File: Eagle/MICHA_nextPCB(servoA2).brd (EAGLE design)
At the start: 110.5 x 83.1 mm, 57 parts, among them IC1 LM4041A12LP, K1 PIN20X2, T1 BSS84, U1 ARDUINO_MKR_ZERO, U2 MIKROE_CLICK, X1 SS-7188S-A-NF_V2, X2 SS-7188S-A-NF_V2, X3 SS-7188S-A-NF_V2, X4 SS-7188S-A-NF_V2, X5 SS-7188S-A-NF_V2, X6 SS-7188S-A-NF_V2, X7 BUCHANAN_4_3.5MM

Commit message: Update for next PCB version
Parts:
- removed TVS3: 5Vdc/12pF, EMCComponents (rev19b):WE-TVS_SOT23-3L
- removed Z3, Z4: 3,3V, Zener_SMA:ZENER_SMA
- added O1: HMHA281R2, HMHA281R2:HMHA281R2
- added R18: 390, resistor:R1206
- added R19: 2k, resistor:R1206
- R1, R2: value 180 -> 100
- R12, R8, R9: device rcl:R1210 -> rcl:R1206
- R6: value 15-1/4W -> 680
- R7: value 15-1/4W -> 1k
- moved R7 54.8 mm to (49.5, 4.76), turned to 0 degrees
- moved R6 39.2 mm to (61.9, -0.95), turned to 180 degrees
- moved R8 11.1 mm to (106.4, -2.70), turned to 0 degrees
- moved Z1 5.29 mm to (99.1, -2.70)
- moved Z2 4.71 mm to (91.1, -2.70)
- moved R9 3.88 mm to (85.4, -0.95), turned to 90 degrees
- moved C6 3.70 mm to (78.7, 0.32)
- moved TBD2 3.70 mm to (78.7, 13.7)
- moved LS1 3.27 mm to (79.4, 35.9)
- moved C3 2.56 mm to (79.1, 46.5)
- moved C4 2.56 mm to (79.1, 50.0)
- moved R3 2.56 mm to (85.4, 46.5)
- moved R4 2.56 mm to (85.4, 50.0)
- moved C5 2.56 mm to (79.1, 53.3)
- moved R5 2.56 mm to (85.4, 53.3)
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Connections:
- removed net N$1: R17.2, T1.2, U1.J5_12
- removed net N$14: C13.1, R6.2, TVS3.2, U1.J4_4, Z3.C
- removed net PUMP_SERVO: R6.1, X4.6
- new net N$7: O1.P$1, R18.2
- new net N$9: C13.1, O1.P$4, R6.1, U1.J4_4
- new net PUMP_SERVO_A+: R18.1, X4.6
- new net PUMP_SERVO_A-: O1.P$2, X4.3
- new net VDD: R17.2, R6.2, T1.2, U1.J5_12
- net D19: now also R19.2; no longer TVS3.1, Z4.C
- net GND: now also O1.P$3, R19.1; no longer TVS3.3, X4.3, Z3.A, Z4.A
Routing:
- net N$14: track 87.9 -> 0.00 mm
- net D19: track 88.9 -> 17.2 mm
- net N$9: track 0.00 -> 67.4 mm, vias 0 -> 2
- net PUMP_ERR: track 2.23 -> 64.7 mm, vias 0 -> 1
- net VDD: track 0.00 -> 55.7 mm, vias 0 -> 1
- net TANK2_RELAY: track 4.79 -> 43.0 mm
- net N$1: track 29.2 -> 0.00 mm
- net N$4: track 18.7 -> 33.7 mm
- net PUMP_SERVO_A-: track 0.00 -> 13.9 mm
- net TX_PI: track 102.5 -> 91.3 mm, vias 1 -> 3
- net PUMP_SERVO_A+: track 0.00 -> 10.8 mm
- net PUMP_DIR: track 3.87 -> 11.3 mm
- net SOL_COLD: track 32.7 -> 39.4 mm
- net D2: track 29.1 -> 24.2 mm
- net PI_STATE_LED: track 38.5 -> 42.7 mm
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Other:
- board text added: "MICHA V1.1"
- board text removed: "MICHA V1.0"

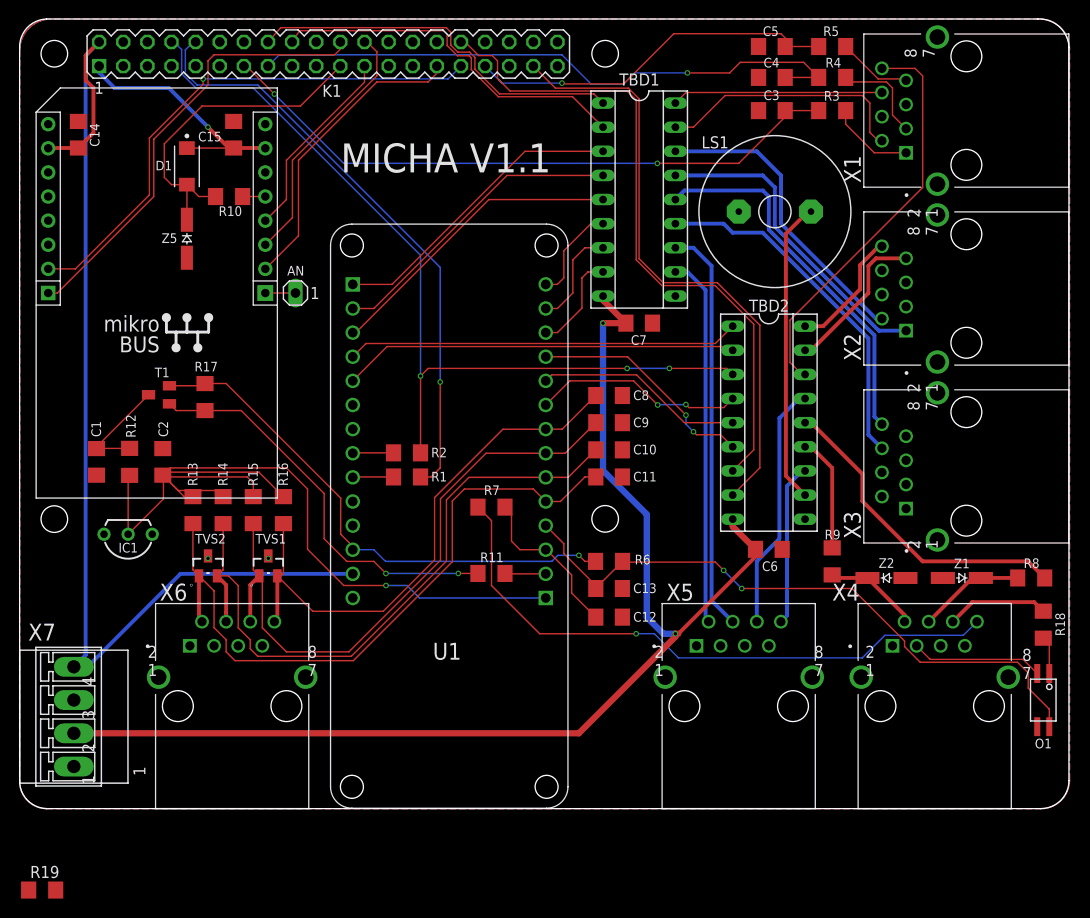
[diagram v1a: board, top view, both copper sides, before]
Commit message: MICHA_nextPCB updated
- analog switch added
- zener and tvs for protection added
- schottky diode deleted
- error signal go through a bridge divider instead of a zener
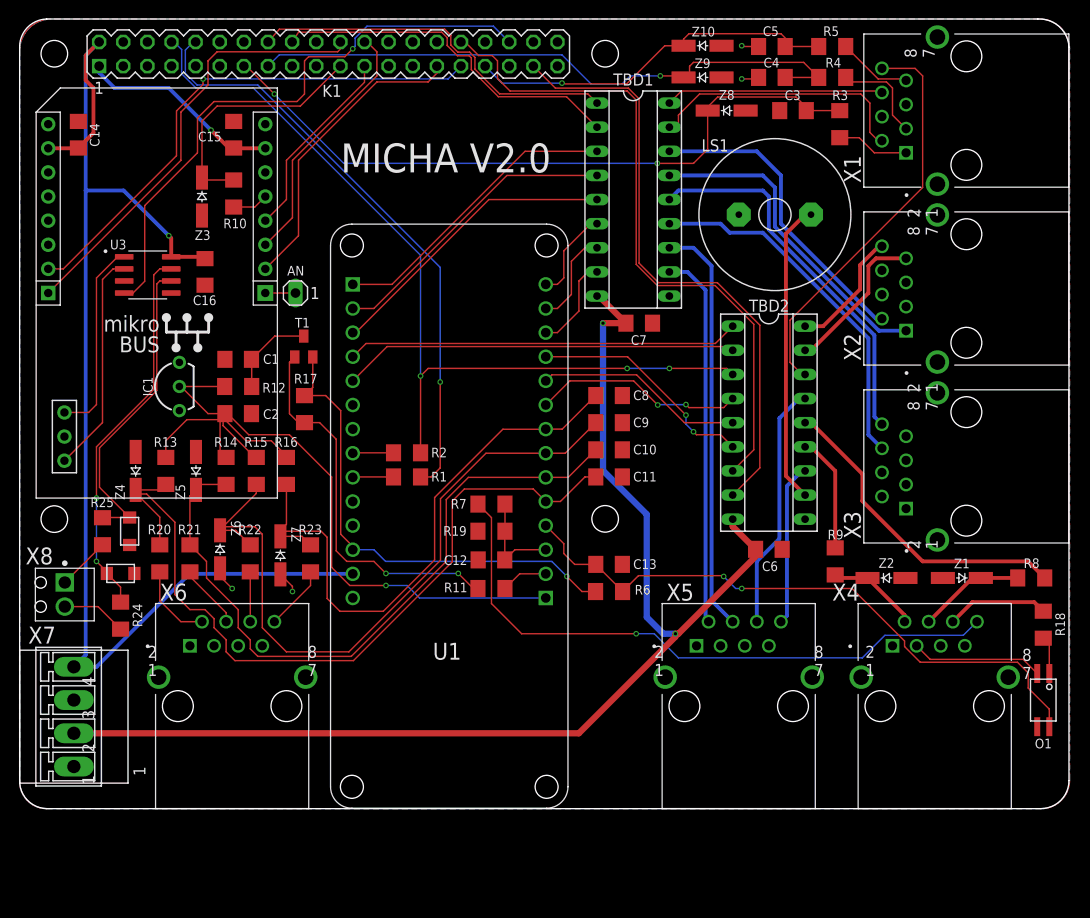
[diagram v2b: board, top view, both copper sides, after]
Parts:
- removed D1: STMICROELECTRONICS_STPS1L30ASTMICROELECTRONICS_STPS1L30A_0_0, Diode_STPS1L30A:STMICROELECTRONICS_STPS1L30A_0
- added C16: 100nF, rcl:C1206
- added R20, R21, R22, R23, R24, R25: 33, resistor:R1206
- added U3: MAX4528CSA, MAX4528CSA:SOIC127P600X175-8N
- added X8: MPT_0,5/_2-2,54_1725656_2, MPT_0_5__2-2_54_1725656:PH_MPT_0,5/_2-2,54_1725656
- added Z10, Z3, Z4, Z6, Z7, Z8, Z9: 3,3V, Zener_SMA:ZENER_SMA
- TVS1, TVS2: value 5Vdc/12pF -> TVS_SOD123; device EMCComponents (rev19b):WE-TVS_SOT23-3L -> TV02W6V0B-G_SOD123:TVS_SOD123
- U2: value MIKROE_CLICK -> MIKROE_CLICK_UPGRADE; device mikrobus_lib:MIKROE_BUS_MIDI_NOLABEL -> mikrobus_lib:MIKROE_BUS_MIDI_UPGRADE
- moved R19 60.5 mm to (49.5, 2.22)
- moved Z5 24.5 mm to (18.4, 8.57), turned to 90 degrees
- moved C1 18.4 mm to (22.9, 20.3), turned to 180 degrees
- moved IC1 16.5 mm to (16.7, 17.5), turned to 90 degrees
- moved T1 16.1 mm to (29.8, 21.7), turned to 0 degrees
- moved TVS1 15.6 mm to (10.5, -2.22), turned to 0 degrees
- moved R12 13.9 mm to (22.9, 17.5), turned to 0 degrees
- moved C12 13.8 mm to (49.5, -0.79), turned to 180 degrees
- moved R17 10.6 mm to (29.8, 15.1)
- moved C2 9.42 mm to (22.9, 14.6), turned to 0 degrees
- moved TVS2 9.03 mm to (11.4, 2.22), turned to 270 degrees
- moved R13 5.02 mm to (15.2, 8.57)
- moved R14 4.14 mm to (21.6, 8.57)
- moved R15 4.14 mm to (24.8, 8.57)
- moved R16 4.14 mm to (27.9, 8.57)
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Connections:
- removed net AN: AN.1, U2.P$1
- removed net MISO: R10.2, U2.P$5
- new net N$1: U2.B, U3.2
- new net N$10: U2.A, U3.1
- new net N$11: C11.1, R13.2, R20.1, U1.J4_5, Z4.C
- new net N$12: C10.1, R14.2, R21.1, U1.J4_6, Z5.C
- new net N$13: C9.1, R15.2, R22.1, U1.J4_7, Z6.C
- new net N$14: C8.1, R16.2, R23.1, U1.J4_8, Z7.C
- new net N$15: R10.2, U2.R_MISO
- new net N$16: AN.1, U2.R_AN
- new net N$17: R24.2, X8.2
- new net N$18: R25.2, X8.1
- new net R_SWITCH: K1.36, U3.4
- new net R_X: R24.1, TVS1.P$1, U3.7
- new net R_Y: R25.1, TVS2.P$1, U3.6
- net +3V3: now also U2.R_3.3V; no longer D1.1, U2.P$7
- net +5V: now also C16.1, U2.R_5V, U3.8; no longer U2.P$10
- net CS: now also U2.R_CS; no longer U2.P$3
- net GND: now also C16.2, TVS1.P$2, TVS2.P$2, U2.R_GND1, U2.R_GND2, U3.3, U3.5, Z10.A, Z3.A, Z4.A, Z6.A, Z7.A, Z8.A, Z9.A; no longer TVS1.3, TVS2.3, U2.P$8, U2.P$9
- net PI_STOP_BTN: now also Z10.C
- net PUMP_PAUSE_BTN: now also Z8.C
- net PUMP_START_BTN: now also Z9.C
- net S1/PWM: now also U2.R_PWM; no longer U2.P$16
- net S2/INT: now also U2.R_INT; no longer U2.P$15
- net S3/RST: now also U2.R_RST; no longer U2.P$2
- net SCK: now also U2.R_SCK; no longer U2.P$4
- net SDO: now also Z3.C; no longer D1.2, Z5.C
- net THERMI1: now also R20.2; no longer C11.1, R13.2, TVS2.1, U1.J4_5
- net THERMI2: now also R21.2; no longer C10.1, R14.2, TVS2.2, U1.J4_6
- net THERMI3: now also R22.2; no longer C9.1, R15.2, TVS1.1, U1.J4_7
- net THERMI4: now also R23.2; no longer C8.1, R16.2, TVS1.2, U1.J4_8
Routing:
- net N$11: track 0.00 -> 85.0 mm
- net N$13: track 0.00 -> 74.8 mm
- net N$12: track 0.00 -> 72.6 mm
- net THERMI1: track 72.1 -> 8.39 mm
- net THERMI2: track 70.3 -> 6.82 mm
- net N$14: track 0.00 -> 63.4 mm
- net R_SWITCH: track 0.00 -> 62.2 mm, vias 0 -> 1
- net THERMI3: track 66.5 -> 5.25 mm
- net THERMI4: track 59.2 -> 6.82 mm
- net R_X: track 0.00 -> 40.2 mm, vias 0 -> 2
- net R_Y: track 0.00 -> 32.9 mm
- net N$1: track 0.00 -> 23.5 mm
- net N$10: track 0.00 -> 20.9 mm
- net +5V: track 116.3 -> 132.9 mm, vias 0 -> 1
- net N$6: track 100.8 -> 87.4 mm
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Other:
- board text added: "MICHA V2.0"
- board text removed: "MICHA V1.1"

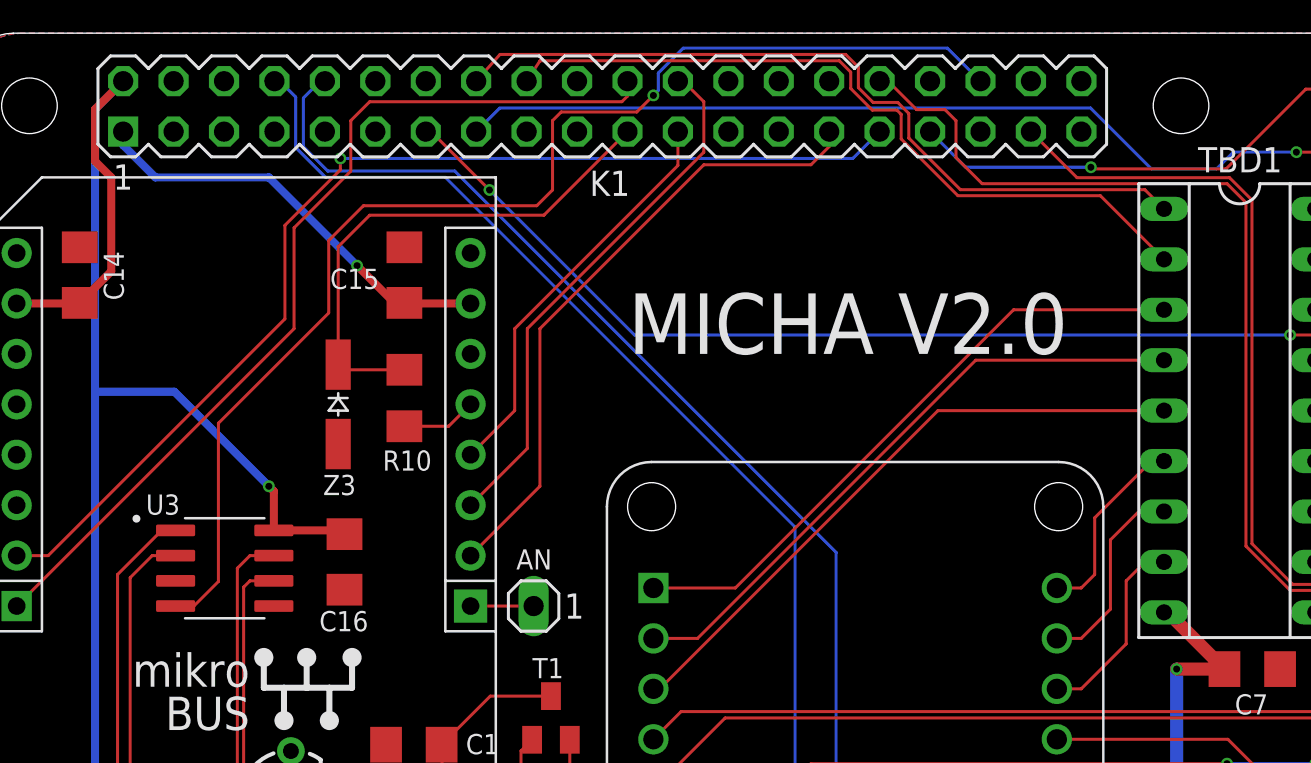
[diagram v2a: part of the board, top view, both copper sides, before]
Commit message: MICHA_nextPCB eagle files updated
3.3V source of Mikro deleted
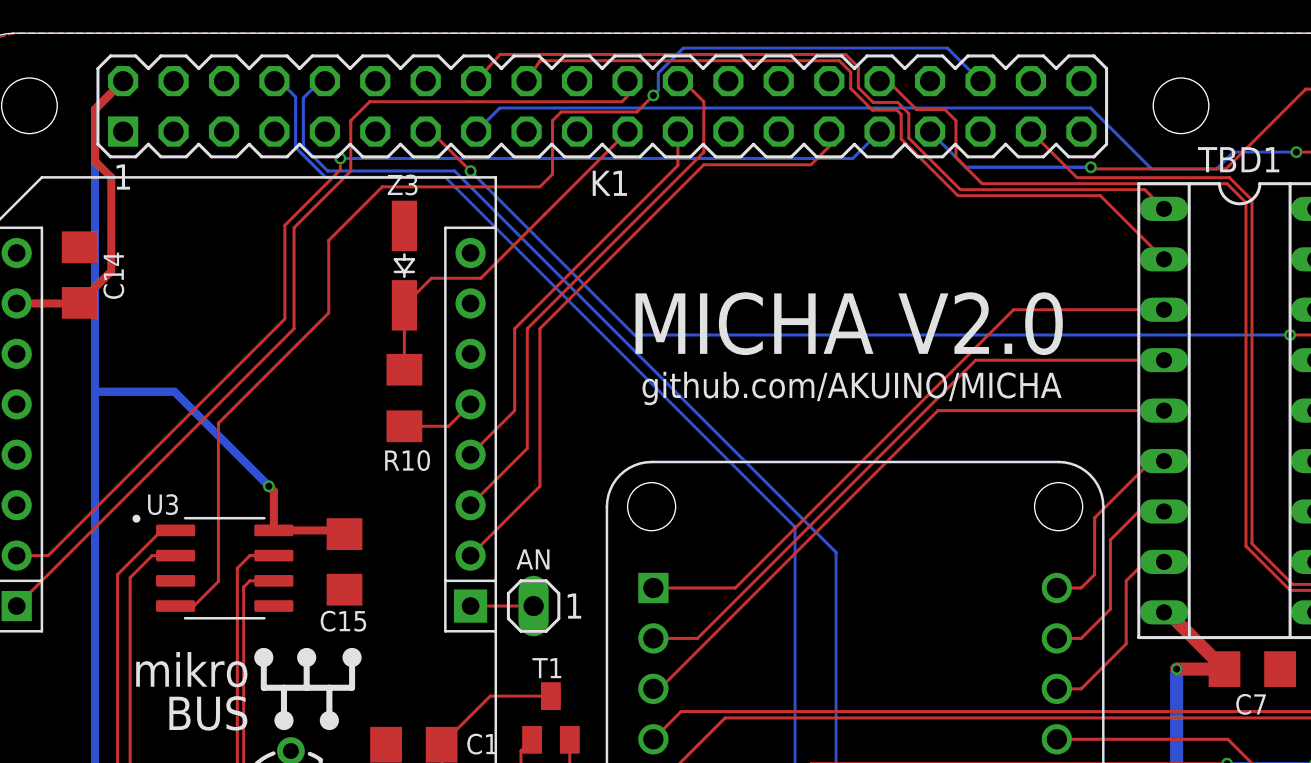
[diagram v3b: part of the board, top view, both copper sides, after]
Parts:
- removed C16: 100nF, rcl:C1206
- moved C15 14.8 mm to (19.4, 29.5), turned to 270 degrees
- moved Z3 7.74 mm to (22.4, 44.5), turned to 90 degrees
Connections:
- removed net +3V3: C15.1, K1.1, U2.R_3.3V
- net +5V: now also C15.1; no longer C16.1
- net GND: no longer C16.2
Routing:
- net +3V3: track 21.5 -> 0.00 mm, vias 1 -> 0
- net SDO: track 26.4 -> 18.1 mm
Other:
- board text added: "github.com/AKUINO/MICHA"
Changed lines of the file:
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@@
 <wire x1="61.515625" y1="-32.22625" x2="61.2775" y2="-32.385" width="0.1524" layer="28"/>
 <wire x1="-0.3175" y1="3.4925" x2="68.2625" y2="3.4925" width="0.1524" layer="37"/>
+<text x="34.29" y="37.7825" size="1.27" layer="25">github.com/AKUINO/MICHA</text>
 </plain>
 <attributes>
@@
 <attribute name="SPICEPREFIX" value="C" x="6.0325" y="43.97375" size="1.778" layer="27" rot="R90" display="off"/>
 </element>
-<element name="C15" library="rcl" library_urn="urn:adsk.eagle:library:334" package="C1206" package3d_urn="urn:adsk.eagle:package:23618/2" value="100nF" x="22.38375" y="43.97375" smashed="yes" rot="R90">
-<attribute name="NAME" x="21.11375" y="44.29125" size="1.016" layer="25" rot="R180"/>
-<attribute name="POPULARITY" value="54" x="22.38375" y="43.97375" size="1.778" layer="27" rot="R90" display="off"/>
-<attribute name="SPICEPREFIX" value="C" x="22.38375" y="43.97375" size="1.778" layer="27" rot="R90" display="off"/>
-</element>
 <element name="U2" library="mikrobus_lib" package="MIKROE_BUS_MIDI_UPGRADE" value="MIKROE_CLICK_UPGRADE" x="26.9875" y="48.895" smashed="yes" rot="R180"/>
 <element name="R10" library="resistor" package="R1206" value="1k" x="22.38375" y="37.7825" smashed="yes" rot="R270">
@@
 <attribute name="NAME" x="90.297" y="-1.635125" size="1.016" layer="25"/>
 </element>
-<element name="Z3" library="Zener_SMA" package="ZENER_SMA" value="3,3V" x="19.05" y="37.465" smashed="yes" rot="R270">
-<attribute name="NAME" x="18.288" y="32.893" size="1.016" layer="25"/>
+<element name="Z3" library="Zener_SMA" package="ZENER_SMA" value="3,3V" x="22.38375" y="44.45" smashed="yes" rot="R90">
+<attribute name="NAME" x="23.14575" y="49.022" size="1.016" layer="25" rot="R180"/>
 </element>
 <element name="T1" library="transistor-small-signal" library_urn="urn:adsk.eagle:library:401" package="SOT23" package3d_urn="urn:adsk.eagle:package:29752/1" value="BSS84" x="29.765625" y="21.669375" smashed="yes">
@@
 <attribute name="NAME" x="70.612" y="54.32425" size="1.016" layer="25"/>
 </element>
-<element name="C16" library="rcl" library_urn="urn:adsk.eagle:library:334" package="C1206" package3d_urn="urn:adsk.eagle:package:23618/2" value="100nF" x="19.3675" y="29.5275" smashed="yes" rot="R270">
+<element name="C15" library="rcl" library_urn="urn:adsk.eagle:library:334" package="C1206" package3d_urn="urn:adsk.eagle:package:23618/2" value="100nF" x="19.3675" y="29.5275" smashed="yes" rot="R270">
 <attribute name="NAME" x="18.0975" y="26.035" size="1.016" layer="25"/>
 <attribute name="POPULARITY" value="54" x="19.3675" y="29.5275" size="1.778" layer="27" rot="R270" display="off"/>
@@
 <contactref element="C13" pad="2"/>
 <contactref element="C14" pad="2"/>
-<contactref element="C15" pad="2"/>
 <contactref element="U2" pad="R_GND2"/>
 <contactref element="U2" pad="R_GND1"/>
@@
 <contactref element="Z9" pad="A"/>
 <contactref element="Z10" pad="A"/>
-<contactref element="C16" pad="2"/>
+<contactref element="C15" pad="2"/>
 <wire x1="20.955" y1="-1.6825" x2="20.955" y2="-2.54" width="0.1524" layer="1"/>
 <wire x1="20.955" y1="-2.54" x2="22.225" y2="-3.81" width="0.1524" layer="1"/>
@@
 <wire x1="17.7373" y1="-2.2652" x2="7.94875" y2="-12.05375" width="0.4064" layer="16"/>
 <contactref element="U3" pad="8"/>
-<contactref element="C16" pad="1"/>
+<contactref element="C15" pad="1"/>
 <wire x1="15.81" y1="31.115" x2="19.18" y2="31.115" width="0.4064" layer="1"/>
 <wire x1="19.18" y1="31.115" x2="19.3675" y2="30.9275" width="0.4064" layer="1"/>
@@
 <via x="66.9925" y="40.9575" extent="1-16" drill="0.35"/>
 <wire x1="66.9925" y1="40.9575" x2="33.9725" y2="40.9575" width="0.1524" layer="16"/>
-<wire x1="33.9725" y1="40.9575" x2="26.67" y2="48.26" width="0.1524" layer="16"/>
-<via x="26.67" y="48.26" extent="1-16" drill="0.35"/>
-<wire x1="26.67" y1="48.26" x2="23.73" y2="51.2" width="0.1524" layer="1"/>
+<wire x1="33.9725" y1="40.9575" x2="25.7175" y2="49.2125" width="0.1524" layer="16"/>
+<via x="25.7175" y="49.2125" extent="1-16" drill="0.35"/>
+<wire x1="25.7175" y1="49.2125" x2="23.73" y2="51.2" width="0.1524" layer="1"/>
 <wire x1="23.73" y1="51.2" x2="23.46" y2="51.2" width="0.1524" layer="1"/>
 <wire x1="86.20125" y1="46.507" x2="86.199309375" y2="46.51375" width="0.1524" layer="1"/>
@@
 <wire x1="29.21" y1="33.3375" x2="25.7175" y2="29.845" width="0.1524" layer="1"/>
 </signal>
-<signal name="+3V3">
-<contactref element="K1" pad="1"/>
-<contactref element="C15" pad="1"/>
-<wire x1="22.38375" y1="42.57375" x2="21.87875" y2="42.57375" width="0.4064" layer="1"/>
-<wire x1="21.87875" y1="42.57375" x2="20.0025" y2="44.45" width="0.4064" layer="1"/>
-<via x="20.0025" y="44.45" extent="1-16" drill="0.35"/>
-<wire x1="20.0025" y1="44.45" x2="15.5575" y2="48.895" width="0.4064" layer="16"/>
-<wire x1="15.5575" y1="48.895" x2="9.8425" y2="48.895" width="0.4064" layer="16"/>
-<wire x1="9.8425" y1="48.895" x2="8.22" y2="50.5175" width="0.4064" layer="16"/>
-<wire x1="8.22" y1="50.5175" x2="8.22" y2="51.2" width="0.4064" layer="16"/>
-<contactref element="U2" pad="R_3.3V"/>
-<wire x1="25.7175" y1="42.545" x2="22.4125" y2="42.545" width="0.4064" layer="1"/>
-<wire x1="22.4125" y1="42.545" x2="22.38375" y2="42.57375" width="0.4064" layer="1"/>
-</signal>
 <signal name="PI33">
 <contactref element="TBD2" pad="8"/>
@@
 <contactref element="Z3" pad="C"/>
 <contactref element="K1" pad="21"/>
-<wire x1="29.41" y1="46.99" x2="33.62" y2="51.2" width="0.1524" layer="1"/>
-<wire x1="29.41" y1="46.99" x2="20.6375" y2="46.99" width="0.1524" layer="1"/>
-<wire x1="20.6375" y1="46.99" x2="19.05" y2="45.4025" width="0.1524" layer="1"/>
-<wire x1="19.05" y1="45.4025" x2="19.05" y2="39.465" width="0.1524" layer="1"/>
-<wire x1="19.05" y1="39.465" x2="19.3105" y2="39.2045" width="0.1524" layer="1"/>
-<wire x1="19.3105" y1="39.2045" x2="22.38375" y2="39.2045" width="0.1524" layer="1"/>
+<wire x1="29.41" y1="46.99" x2="29.46875" y2="47.04875" width="0.1524" layer="1"/>
+<wire x1="29.46875" y1="47.04875" x2="33.62" y2="51.2" width="0.1524" layer="1"/>
+<wire x1="22.38375" y1="42.45" x2="22.38375" y2="39.2045" width="0.1524" layer="1"/>
+<wire x1="29.41" y1="46.99" x2="26.235" y2="43.815" width="0.1524" layer="1"/>
+<wire x1="23.74875" y1="43.815" x2="22.38375" y2="42.45" width="0.1524" layer="1"/>
+<wire x1="26.235" y1="43.815" x2="23.74875" y2="43.815" width="0.1524" layer="1"/>
 </signal>
 <signal name="N$3">
@@
 <wire x1="13.0175" y1="36.5125" x2="18.57375" y2="42.06875" width="0.1524" layer="1"/>
 <wire x1="18.57375" y1="42.06875" x2="18.57375" y2="45.72" width="0.1524" layer="1"/>
-<wire x1="18.57375" y1="45.72" x2="20.32" y2="47.46625" width="0.1524" layer="1"/>
-<wire x1="20.32" y1="47.46625" x2="29.05125" y2="47.46625" width="0.1524" layer="1"/>
-<wire x1="29.05125" y1="47.46625" x2="29.845" y2="48.26" width="0.1524" layer="1"/>
-<wire x1="29.845" y1="48.26" x2="29.845" y2="51.7525" width="0.1524" layer="1"/>
+<wire x1="18.57375" y1="45.72" x2="21.2725" y2="48.41875" width="0.1524" layer="1"/>
+<wire x1="21.2725" y1="48.41875" x2="29.21" y2="48.41875" width="0.1524" layer="1"/>
+<wire x1="29.21" y1="48.41875" x2="29.845" y2="49.05375" width="0.1524" layer="1"/>
+<wire x1="29.845" y1="49.05375" x2="29.845" y2="51.7525" width="0.1524" layer="1"/>
 <wire x1="29.845" y1="51.7525" x2="30.2807" y2="52.1882" width="0.1524" layer="1"/>
 <wire x1="34.0907" y1="52.1882" x2="34.925" y2="53.0225" width="0.1524" layer="1"/>
